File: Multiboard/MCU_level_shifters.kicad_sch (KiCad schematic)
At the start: 40 parts, among them Q1 Q_Dual_NMOS_G1S2G2D2S1D1, Q2 Q_Dual_NMOS_G1S2G2D2S1D1, Q3 Q_Dual_NMOS_G1S2G2D2S1D1, Q4 Q_Dual_NMOS_G1S2G2D2S1D1, Q5 Q_Dual_NMOS_G1S2G2D2S1D1, Q6 Q_Dual_NMOS_G1S2G2D2S1D1, Q7 Q_Dual_NMOS_G1S2G2D2S1D1, SW3 SW_SPST, SW4 SW_SPST, SW5 SW_SPST, SW6 SW_SPST, SW8 SW_SPST

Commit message: cleared part of errors and warnings
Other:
- company: (none) -> Technological School "Electronic Systems"
- title: (none) -> IR-Multiboard/MCU_Level_Shifters
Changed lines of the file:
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@@
 	(generator_version "9.0")
 	(paper "A3")
+	(title_block
+		(title "IR-Multiboard/MCU_Level_Shifters")
+		(date "2026-02-23")
+		(company "Technological School \"Electronic Systems\"")
+	)
 	(text "SPI1"
 		(exclude_from_sim no)

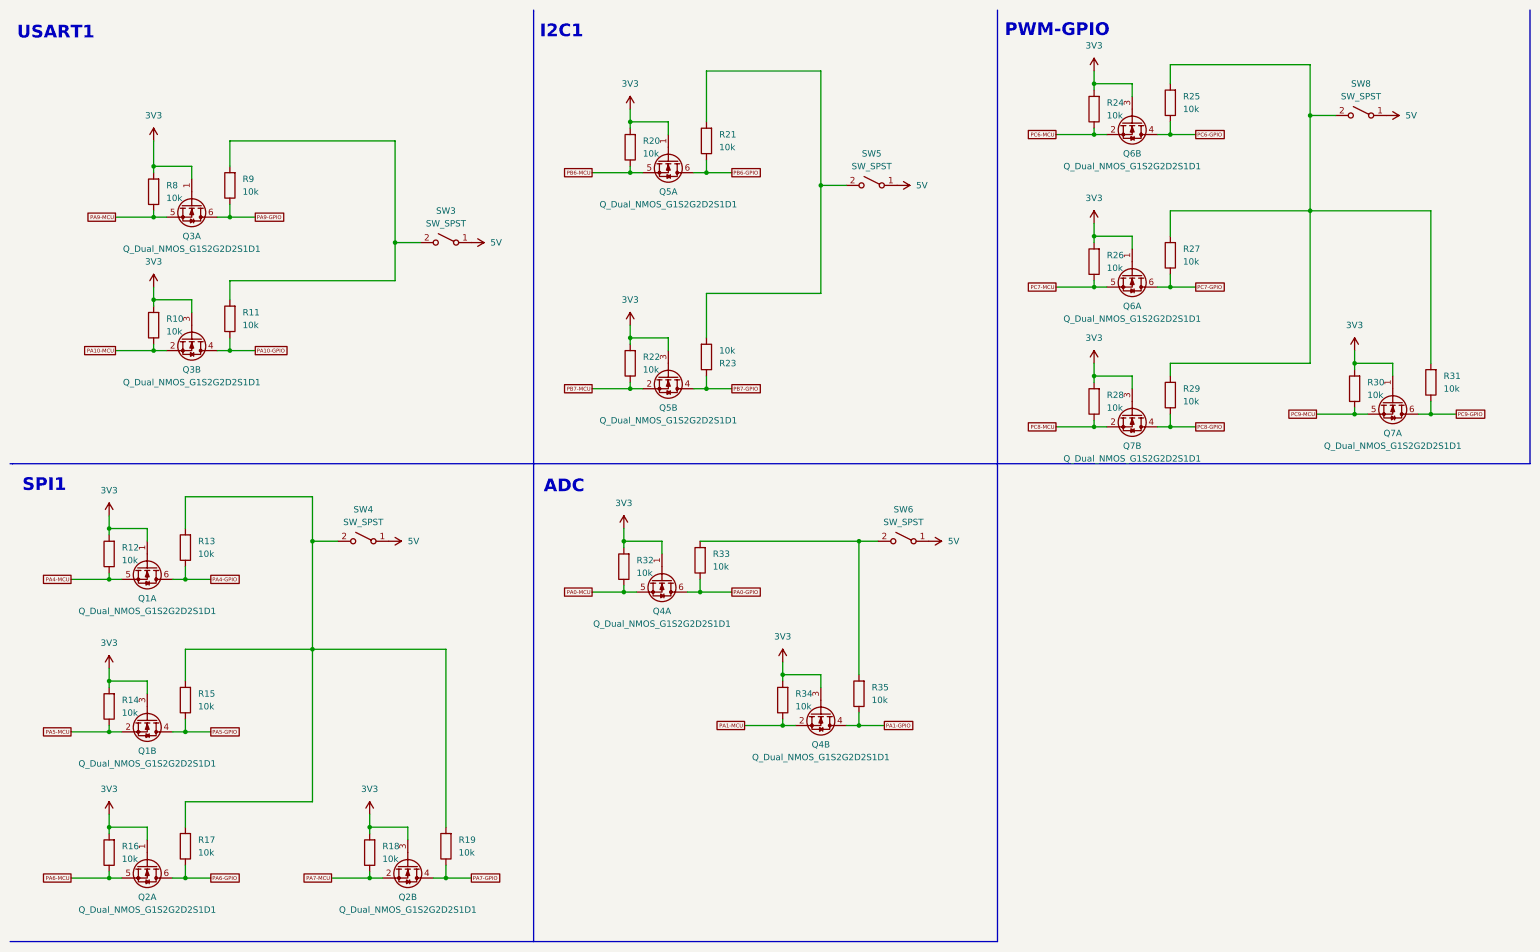
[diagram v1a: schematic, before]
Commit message: fixed dead copper zones and cleared all errors
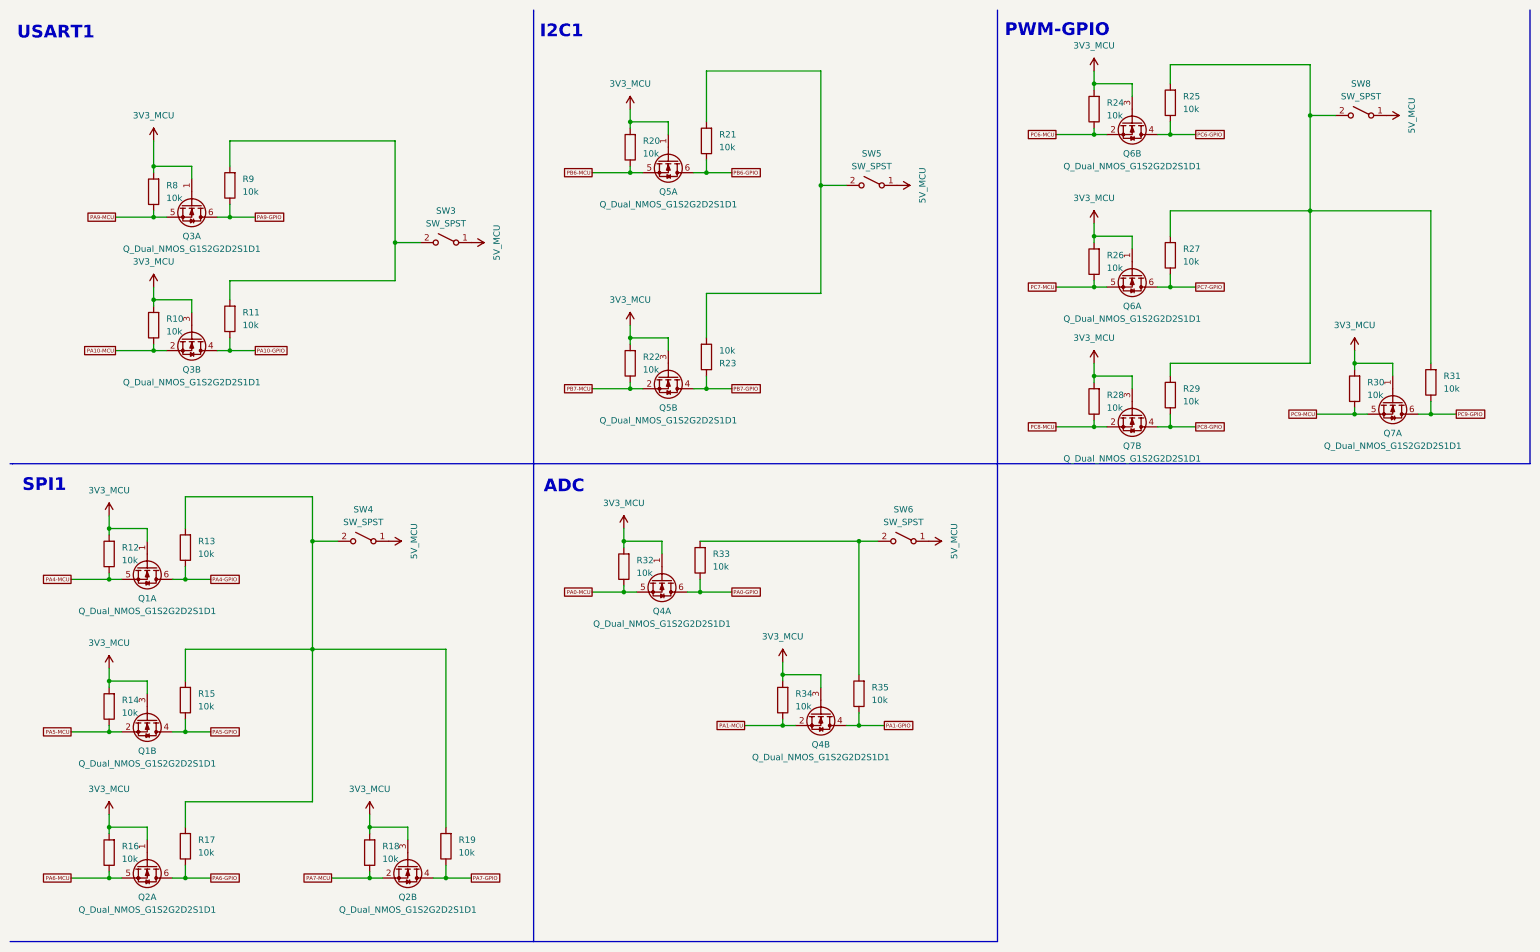
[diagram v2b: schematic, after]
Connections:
- net 3V3 renamed 3V3_MCU
- net 5V renamed 5V_MCU

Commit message: Generated BOM
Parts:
- Q1, Q2, Q3, Q4, Q5, Q6, Q7: LCSC Part Number (none) -> C404322
- R10, R11, R12, R13, R14, R15, R16, R17, R18, R19, R20, R21, R22, R23, R24, R25, R26, R27, R28, R29, R30, R31, R32, R33, R34, R35, R8, R9: LCSC Part Number (none) -> C98220
- SW3, SW4, SW5, SW6, SW8: LCSC Part Number (none) -> C41381904
